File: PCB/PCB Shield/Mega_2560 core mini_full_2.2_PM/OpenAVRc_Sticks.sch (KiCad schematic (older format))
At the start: 58 parts, among them P11 Trim, P12 Stick_left, P13 Stick_right, P14 Switch, P23 Rot_1, P24 Rot_2, P25 Keys, P28 5v/3,3v manches, P31 Pot2, P32 Pot1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

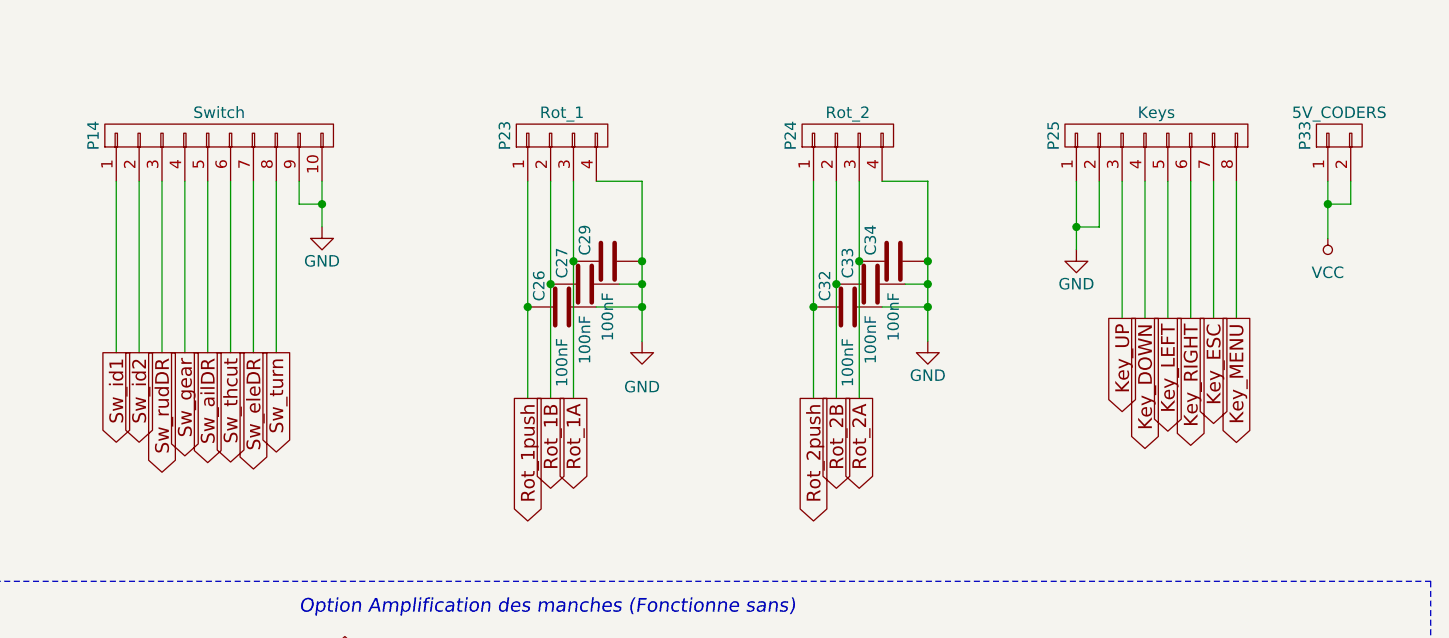
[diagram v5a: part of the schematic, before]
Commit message: Add bitmaps in schematics files for fun.
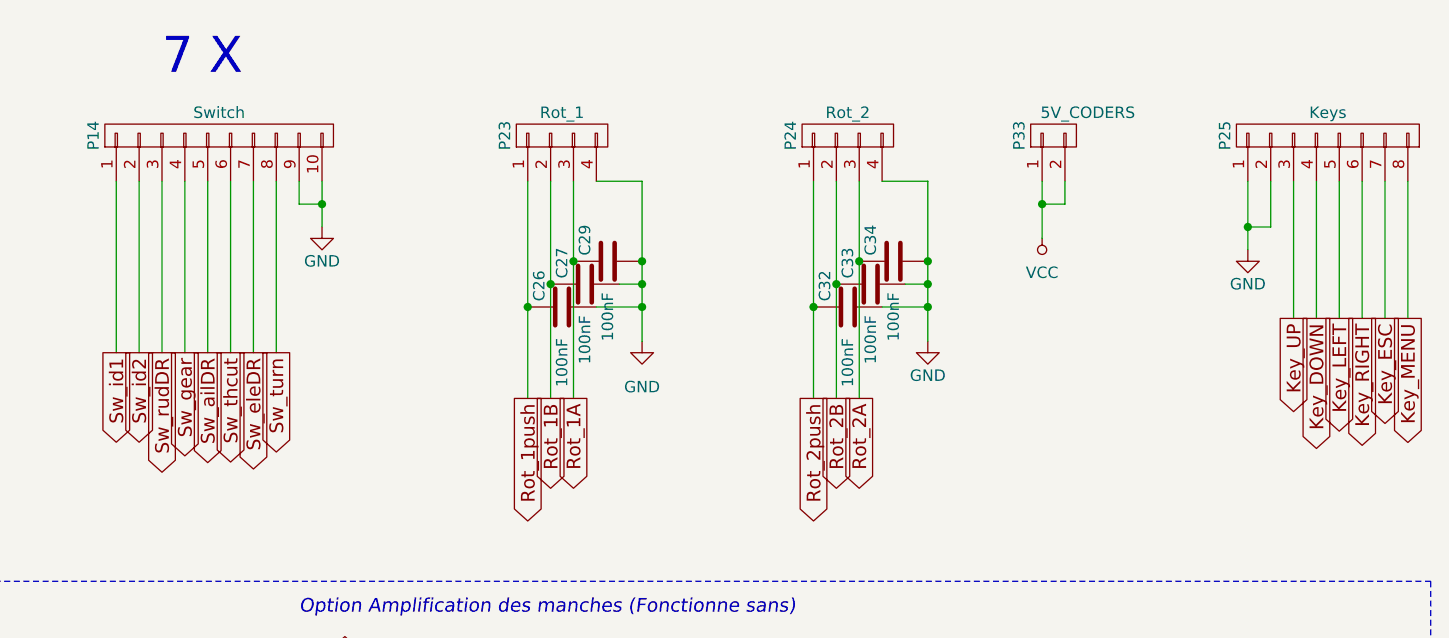
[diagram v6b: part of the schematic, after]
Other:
- note added: "7 X"
- moved on the sheet: P25, P33
